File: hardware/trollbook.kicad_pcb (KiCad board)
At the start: 2 copper layers, 100 x 100 mm, 37 parts, among them K1 CONN_3, P1 VGA, P2 LCD, P3 SPI, U1 XC95288-208, U10 74LS574, U11 74LS574, U12 HY57V561620, U13 HY57V561620, U15 74HC4002, U16 ADA4851-4, U17 DAC0800, U18 DAC0800, U19 74HC139, U2 MC68030, U20 74HC10, U3 MC68882, U4 IDT71V416, U6 74LS574, U7 39F040, U9 74LS574, Y1 50 MHz, Y2 12.288 MHz

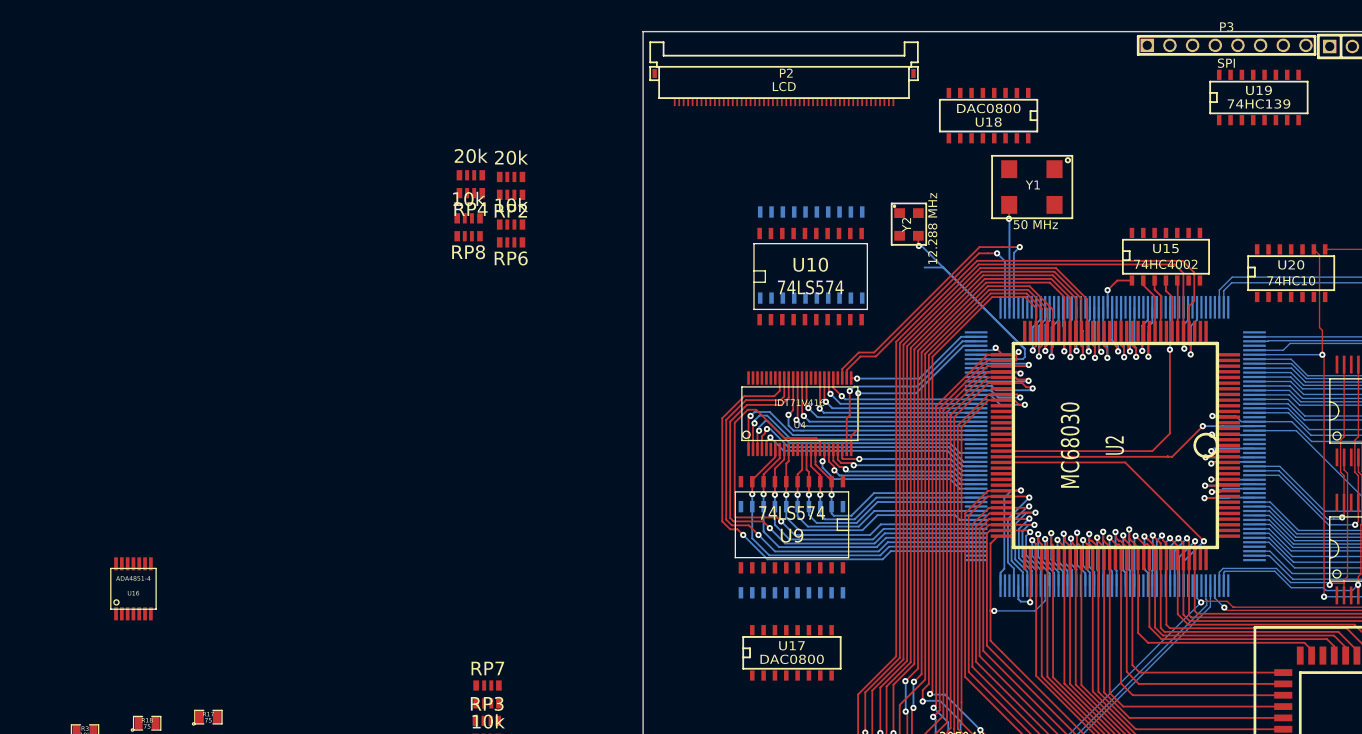
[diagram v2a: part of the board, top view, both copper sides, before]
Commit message: moved sram closer to cpu
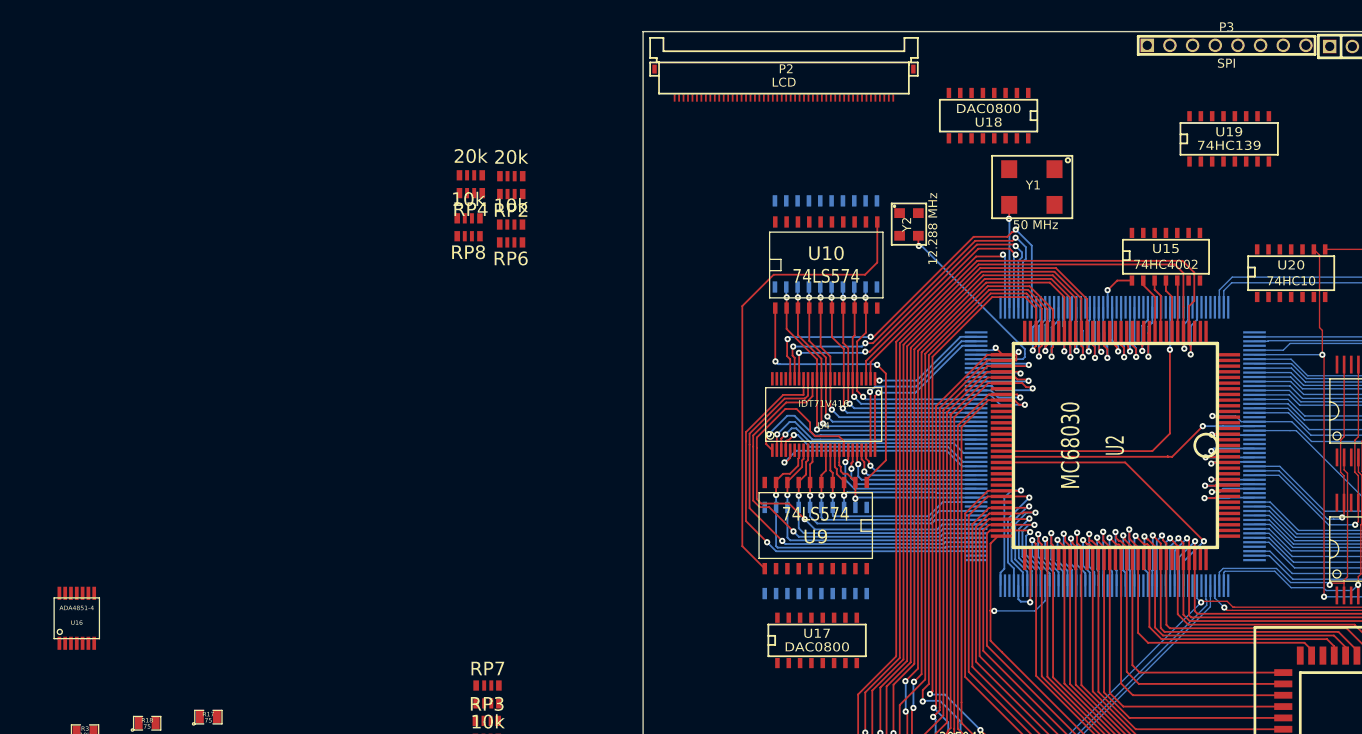
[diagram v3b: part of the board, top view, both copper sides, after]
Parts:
- moved U16 7.16 mm to (26.5, 205.7)
- moved U19 5.71 mm to (155.7, 152.0)
- moved U17 3.15 mm to (109.5, 208.2)
- moved U4 2.67 mm to (110.2, 182.9)
- moved U9 2.67 mm to (109.3, 195.4)
- moved U6 2.67 mm to (109.3, 198.1)
- moved U10 2.18 mm to (110.5, 166.2)
- moved U11 2.07 mm to (110.5, 163.8)
- moved P2 0.50 mm to (118.0, 147.0)
- moved RP2 0.09 mm to (75.2, 157.2)
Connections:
- U1 pad 15: /LLD6 -> /LLD7
- U1 pad 16: /LLD7 -> /LLD6
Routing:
- net /VGALATCH: track 0.00 -> 52.2 mm
- net /LLA18: track 0.00 -> 44.7 mm, vias 0 -> 3
- net /LLA17: track 0.00 -> 42.2 mm, vias 0 -> 3
- net /LLA16: track 0.00 -> 39.6 mm, vias 0 -> 3
- net /VGAOE: track 0.00 -> 32.0 mm, vias 0 -> 2
- net /CLK12: track 39.3 -> 24.3 mm
- net /LLD14: track 25.2 -> 33.8 mm, vias 1 -> 2
- net /LLD15: track 26.8 -> 35.3 mm, vias 1 -> 2
- net /LLD13: track 23.9 -> 32.3 mm, vias 1 -> 2
- net /LLD11: track 21.2 -> 29.4 mm, vias 1 -> 2
- net /LLD8: track 17.6 -> 25.8 mm, vias 1 -> 2
- net /LLD12: track 22.7 -> 30.8 mm, vias 1 -> 2
- net /LLD10: track 19.9 -> 27.8 mm, vias 1 -> 2
- net /LLD9: track 18.6 -> 26.5 mm, vias 1 -> 2
- net /LLBLE: track 49.9 -> 44.5 mm
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
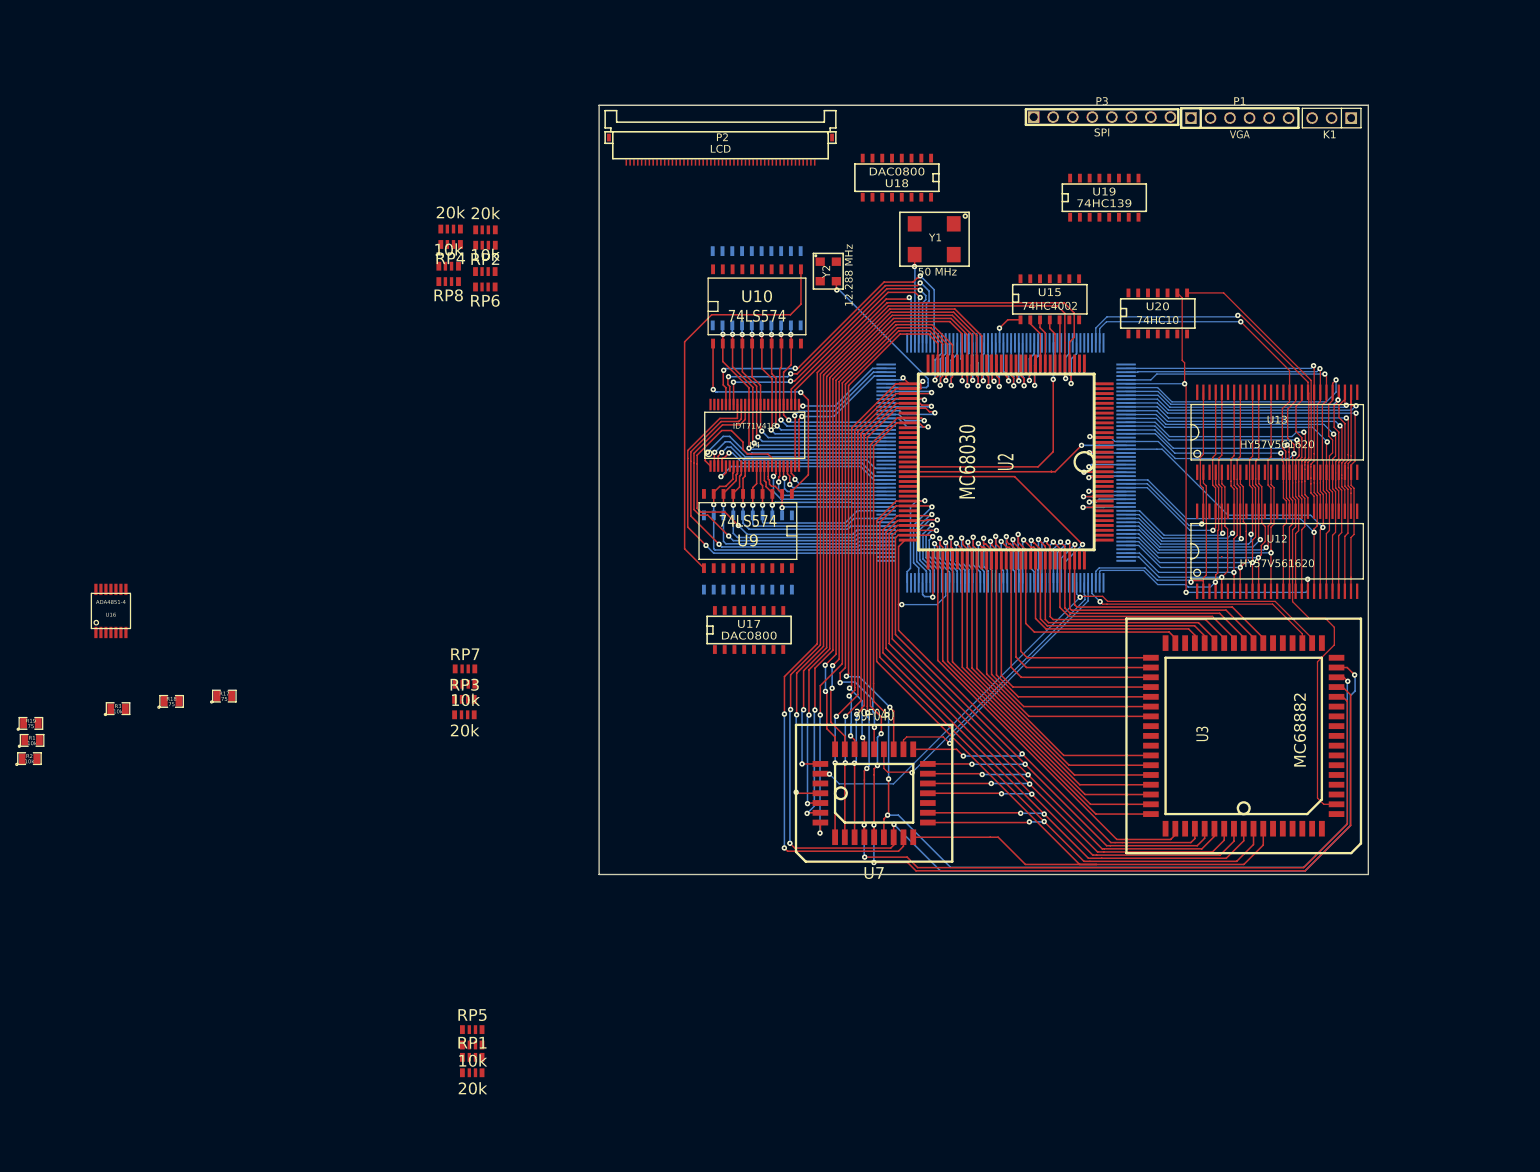
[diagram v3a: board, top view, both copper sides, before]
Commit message: lcd connector, vga dac
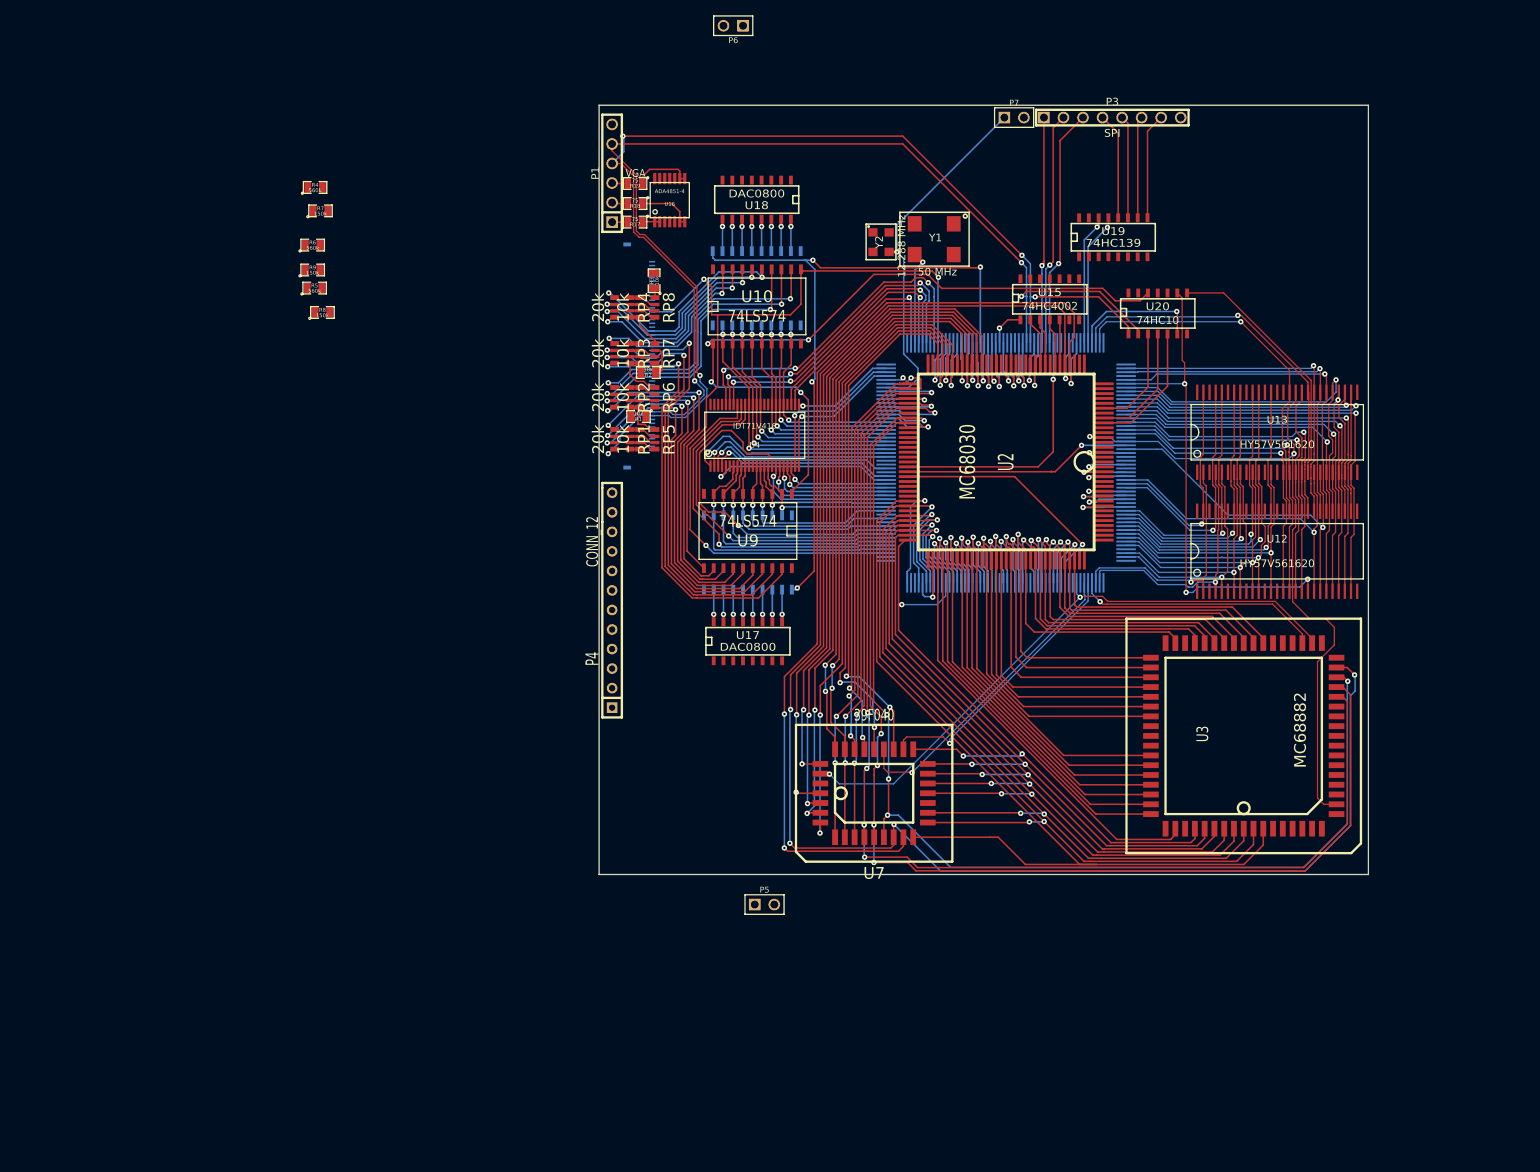
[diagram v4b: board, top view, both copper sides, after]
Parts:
- removed K1: CONN_3, PIN_ARRAY_3X1
- added P4: CONN_12, SIL-12, F.Cu at (91.7, 204.3)
- added P5: CONN_2, PIN_ARRAY_2X1, F.Cu at (111.5, 243.9)
- added P6: CONN_2, PIN_ARRAY_2X1, F.Cu at (107.4, 129.7)
- added P7: CONN_2, PIN_ARRAY_2X1, F.Cu at (144.0, 141.6)
- added R4: 560k, SM0805, F.Cu at (53.1, 150.7)
- added R5: 560k, SM0805, F.Cu at (53.0, 163.8)
- added R6: 560k, SM0805, F.Cu at (52.8, 158.2)
- added R7: 150k, SM0805, F.Cu at (53.8, 153.7)
- added R8: 150k, SM0805, F.Cu at (54.0, 166.9)
- added R9: 150k, SM0805, F.Cu at (52.8, 161.4)
- P2: moved to B.Cu
- moved R19 105.3 mm to (94.7, 150.2), turned to 180 degrees
- moved R2 94.8 mm to (96.4, 174.8), turned to 180 degrees
- moved U16 90.2 mm to (99.2, 152.3)
- moved R1 89.4 mm to (95.1, 180.5), turned to 180 degrees
- moved R3 89.2 mm to (97.2, 162.8), turned to 90 degrees
- moved R18 88.4 mm to (94.7, 152.8), turned to 180 degrees
- moved RP1 83.6 mm to (93.0, 183.5), turned to 270 degrees
- moved P1 81.9 mm to (91.7, 148.8), turned to 90 degrees
- moved R17 81.5 mm to (94.7, 155.2), turned to 180 degrees
- moved RP5 81.0 mm to (96.3, 183.5), turned to 270 degrees
- moved RP3 50.3 mm to (93.0, 172.3), turned to 270 degrees
- moved RP7 48.2 mm to (96.3, 172.3), turned to 270 degrees
- moved P2 43.6 mm to (96.4, 184.8), turned to 90 degrees
- moved RP2 27.4 mm to (93.0, 178.0), turned to 270 degrees
- moved RP8 26.2 mm to (96.3, 166.3), turned to 270 degrees
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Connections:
- P2 pad 1: (no net) -> +10V
- P2 pad 10: (no net) -> /VGAVSYNC
- P2 pad 11: (no net) -> /VGAHSYNC
- P2 pad 12: (no net) -> /VGAB4
- P2 pad 13: (no net) -> /VGAB3
- P2 pad 14: (no net) -> /VGAB2
- P2 pad 15: (no net) -> /VGAB1
- P2 pad 16: (no net) -> /VGAB0
- P2 pad 17: (no net) -> GND
- P2 pad 18: (no net) -> GND
- P2 pad 19: (no net) -> GND
- P2 pad 2: (no net) -> +10V
- P2 pad 20: (no net) -> /VGAG5
- P2 pad 21: (no net) -> /VGAG4
- P2 pad 22: (no net) -> /VGAG3
- P2 pad 23: (no net) -> /VGAG2
- P2 pad 24: (no net) -> /VGAG1
- P2 pad 25: (no net) -> /VGAG0
- P2 pad 26: (no net) -> GND
- P2 pad 27: (no net) -> GND
- P2 pad 28: (no net) -> /VGAR4
- P2 pad 29: (no net) -> /VGAR3
- P2 pad 3: (no net) -> GND
- P2 pad 30: (no net) -> /VGAR2
- P2 pad 31: (no net) -> /VGAR1
- P2 pad 32: (no net) -> /VGAR0
- P2 pad 33: (no net) -> GND
- P2 pad 34: (no net) -> GND
- P2 pad 35: (no net) -> GND
- P2 pad 36: (no net) -> GND
- P2 pad 37: (no net) -> /VGALATCH
- P2 pad 38: (no net) -> GND
- P2 pad 39: (no net) -> 3V3
- P2 pad 4: (no net) -> GND
- P2 pad 40: (no net) -> GND
- P2 pad 41: (no net) -> +15V
- P2 pad 42: (no net) -> -10V
- P2 pad 43: (no net) -> +5V
- P2 pad 5: (no net) -> GND
- P2 pad 7: (no net) -> 3V3
- P2 pad 8: (no net) -> GND
- RP1 pad 1: N-00000224 -> N-00000228
- RP2 pad 2: N-0000064 -> N-00000186
- RP3 pad 4: N-0000065 -> N-00000175
- RP5 pad 8: N-00000224 -> N-00000228
- RP6 pad 7: N-0000064 -> N-00000186
- RP7 pad 5: N-0000065 -> N-00000175
- U10 pad 20: VCC -> 3V3
- U11 pad 20: VCC -> 3V3
- U15 pad 14: +5V -> 3V3
- U16 pad 10: N-0000065 -> N-00000127
- U16 pad 3: N-00000224 -> N-00000159
- U16 pad 5: N-0000064 -> N-00000126
- U17 pad 6: (no net) -> N-00000123
- U17 pad 8: (no net) -> N-00000122
- U18 pad 6: (no net) -> N-00000124
- U18 pad 8: (no net) -> N-00000125
- U19 pad 16: VCC -> 3V3
- U20 pad 10: +5V -> 3V3
- U20 pad 11: +5V -> 3V3
- U20 pad 13: +5V -> 3V3
- U20 pad 14: VCC -> 3V3
- U3 pad 14: /RESET -> GND
- U6 pad 20: VCC -> 3V3
- U7 pad 16: (no net) -> GND
- U7 pad 32: (no net) -> +5V
- U9 pad 20: VCC -> 3V3
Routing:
- net /VGAVSYNC: track 0.00 -> 135.6 mm, vias 0 -> 3
- net /VGAHSYNC: track 0.00 -> 133.7 mm, vias 0 -> 4
- net /SNDLATCH: track 0.00 -> 91.3 mm, vias 0 -> 4
- net /VGAOE: track 32.0 -> 95.3 mm, vias 2 -> 4
- net /VGAG0: track 0.00 -> 58.2 mm, vias 0 -> 2
- net /VGAG1: track 0.00 -> 57.6 mm, vias 0 -> 2
- net /VGAG2: track 0.00 -> 57.2 mm, vias 0 -> 2
- net /VGAB4: track 0.00 -> 46.7 mm, vias 0 -> 2
- net /VGAB3: track 0.00 -> 45.3 mm, vias 0 -> 2
- net /VGAB2: track 0.00 -> 44.1 mm, vias 0 -> 2
- net /VGAB1: track 0.00 -> 43.0 mm, vias 0 -> 2
- net /VGAB0: track 0.00 -> 41.8 mm, vias 0 -> 2
- net /VGALATCH: track 52.2 -> 92.6 mm, vias 0 -> 2
- net /VGAG3: track 0.00 -> 36.6 mm, vias 0 -> 2
- net /VGAG4: track 0.00 -> 36.5 mm, vias 0 -> 2
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
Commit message: 3d models
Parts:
- moved R4 26.3 mm to (78.5, 157.4)
- moved R8 26.3 mm to (79.4, 173.7)
- moved R5 26.3 mm to (78.4, 170.5)
- moved R7 26.3 mm to (79.2, 160.5)
- moved R6 26.3 mm to (78.2, 164.9)
- moved R9 26.3 mm to (78.2, 168.1)
- moved P6 5.22 mm to (107.8, 134.9)
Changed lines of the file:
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@@
     (links 648)
     (no_connects 213)
-    (area 89.924999 139.924999 190.075001 240.075001)
+    (area 76.137769 102.362 232.534333 245.452901)
     (thickness 1.6)
     (drawings 8)
@@
   )
   (setup
-    (last_trace_width 0.2032)
+    (last_trace_width 0.1524)
     (user_trace_width 0.1524)
     (user_trace_width 0.2032)
@@
     (visible_elements FFFFFFCF)
     (pcbplotparams
-      (layerselection 3178497)
-      (usegerberextensions true)
+      (layerselection 32769)
+      (usegerberextensions false)
       (excludeedgelayer true)
       (linewidth 0.150000)
@@
       (padsonsilk false)
       (subtractmaskfromsilk false)
-      (outputformat 1)
+      (outputformat 2)
       (mirror false)
-      (drillshape 1)
+      (drillshape 0)
       (scaleselection 1)
-      (outputdirectory ""))
+      (outputdirectory /tmp/orvar/))
   )
   (net 0 "")
@@
       (net 86 /IPL1)
     )
+    (model 3d/pqfp132.wrl
+      (at (xyz 0 0 0))
+      (scale (xyz 1 1 1))
+      (rotate (xyz 0 0 90))
+    )
   )
   (module PLCC68MS (layer F.Cu)
@@
       (net 3 +5V)
     )
+    (model 3d/plcc68.wrl
+      (at (xyz 0 0 0))
+      (scale (xyz 1 1 1))
+      (rotate (xyz 0 0 0))
+    )
   )
   (module TSSOP-48 (layer F.Cu)
@@
       (net 3 +5V)
     )
+    (model 3d/plcc32.wrl
+      (at (xyz 0 0 0))
+      (scale (xyz 1 1 1))
+      (rotate (xyz 0 0 90))
+    )
   )
   (module SM0805 (layer F.Cu)
@@
   )
   (module PIN_ARRAY_2X1 (layer F.Cu)
-    (at 107.442 129.667 180)
+    (at 107.823 134.874 180)
     (descr "Connecteurs 2 pins")
     (tags "CONN DEV")
@@
   )
   (module SM0805 (layer F.Cu)
-    (at 54.0385 166.9415)
+    (at 79.4385 173.6725)
     (attr smd)
     (fp_text reference R8 (at 0 -0.3175) (layer F.SilkS)
@@
   )
   (module SM0805 (layer F.Cu)
-    (at 52.7685 158.1785)
+    (at 78.1685 164.9095)
     (attr smd)
     (fp_text reference R6 (at 0 -0.3175) (layer F.SilkS)
@@
   )
   (module SM0805 (layer F.Cu)
-    (at 52.7685 161.417)
+    (at 78.1685 168.148)
     (attr smd)
     (fp_text reference R9 (at 0 -0.3175) (layer F.SilkS)
@@
   )
   (module SM0805 (layer F.Cu)
-    (at 53.0225 163.7665)
+    (at 78.4225 170.4975)
     (attr smd)
     (fp_text reference R5 (at 0 -0.3175) (layer F.SilkS)
@@
   )
   (module SM0805 (layer F.Cu)
-    (at 53.7845 153.7335)
+    (at 79.1845 160.4645)
     (attr smd)
     (fp_text reference R7 (at 0 -0.3175) (layer F.SilkS)
@@
   )
   (module SM0805 (layer F.Cu)
-    (at 53.086 150.6855)
+    (at 78.486 157.4165)
     (attr smd)
     (fp_text reference R4 (at 0 -0.3175) (layer F.SilkS)

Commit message: ostkaka
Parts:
- removed U17, U18: DAC0800, SO16E
- added U5: TLC7524, SO16E, F.Cu at (108.8, 212.0)
- added U8: TLC7524, SO16E, F.Cu at (111.3, 151.3)
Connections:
- P5 pad 1: N-00000123 (its old number) -> GND
- P6 pad 1: N-00000124 (its old number) -> GND
- U1 pad 176: (no net) -> N-00000122
- U1 pad 94: (no net) -> N-00000120
- U1 pad 96: (no net) -> N-00000119
- U1 pad 98: (no net) -> N-00000121
- U3 pad 14: GND -> /RESET
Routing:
- net N-00000137: track 4.17 -> 0.00 mm, vias 1 -> 0
- net N-00000128: track 4.17 -> 0.00 mm, vias 1 -> 0
- net N-00000127: track 4.17 -> 0.00 mm, vias 1 -> 0
- net N-00000126: track 4.17 -> 0.00 mm, vias 1 -> 0
- net N-00000125: track 4.17 -> 0.00 mm, vias 1 -> 0
- net N-00000124: track 4.17 -> 0.00 mm, vias 1 -> 0
- net N-00000111: track 4.17 -> 0.00 mm, vias 1 -> 0
- net N-00000108: track 4.17 -> 0.00 mm, vias 1 -> 0
- net N-00000132: track 4.15 -> 0.00 mm, vias 1 -> 0
- net N-00000117: track 4.15 -> 0.00 mm, vias 1 -> 0
- net N-00000116: track 4.15 -> 0.00 mm, vias 1 -> 0
- net N-00000115: track 4.15 -> 0.00 mm, vias 1 -> 0
- net N-00000114: track 4.15 -> 0.00 mm, vias 1 -> 0
- net N-00000113: track 4.15 -> 0.00 mm, vias 1 -> 0
- net N-00000112: track 4.15 -> 0.00 mm, vias 1 -> 0
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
